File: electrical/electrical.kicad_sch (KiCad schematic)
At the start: 29 parts, among them J1 Raspberry Pi GPIO, J2 Touch screen connector, J3 Load_cell, J4 PIR_sensor, J9 Water_sensor, K1 RAYEX-L90, M1 Milk_powder, M2 Instant_coffee, M3 Sugar, M4 Motor_DC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

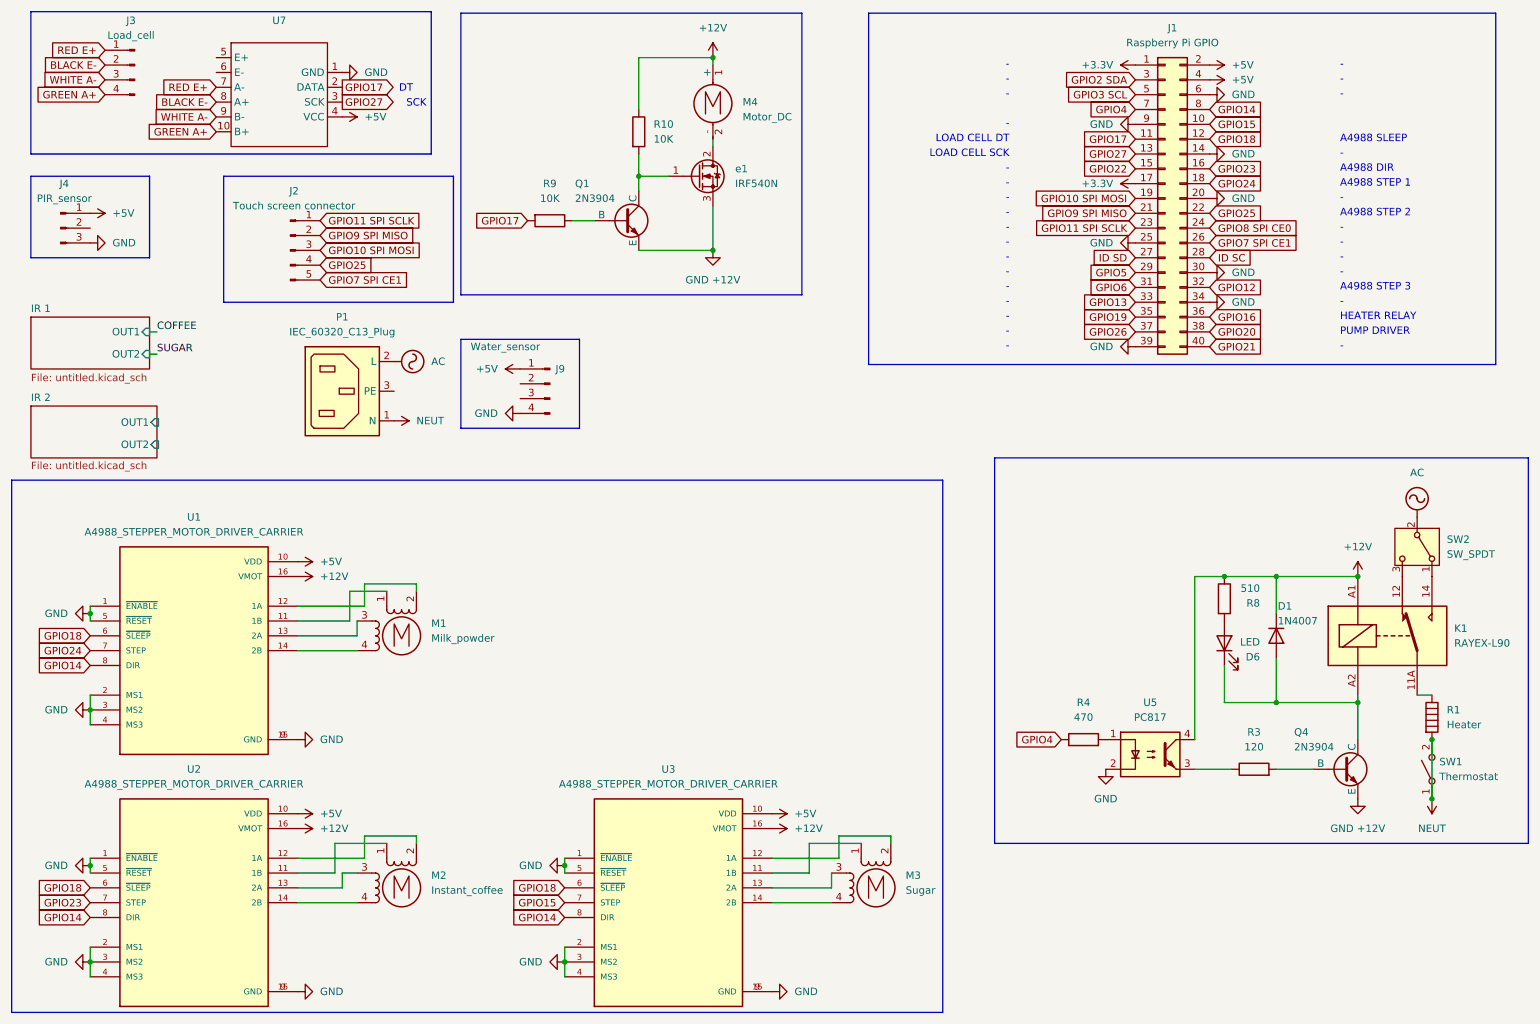
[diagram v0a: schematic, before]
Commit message: added scrolling feature
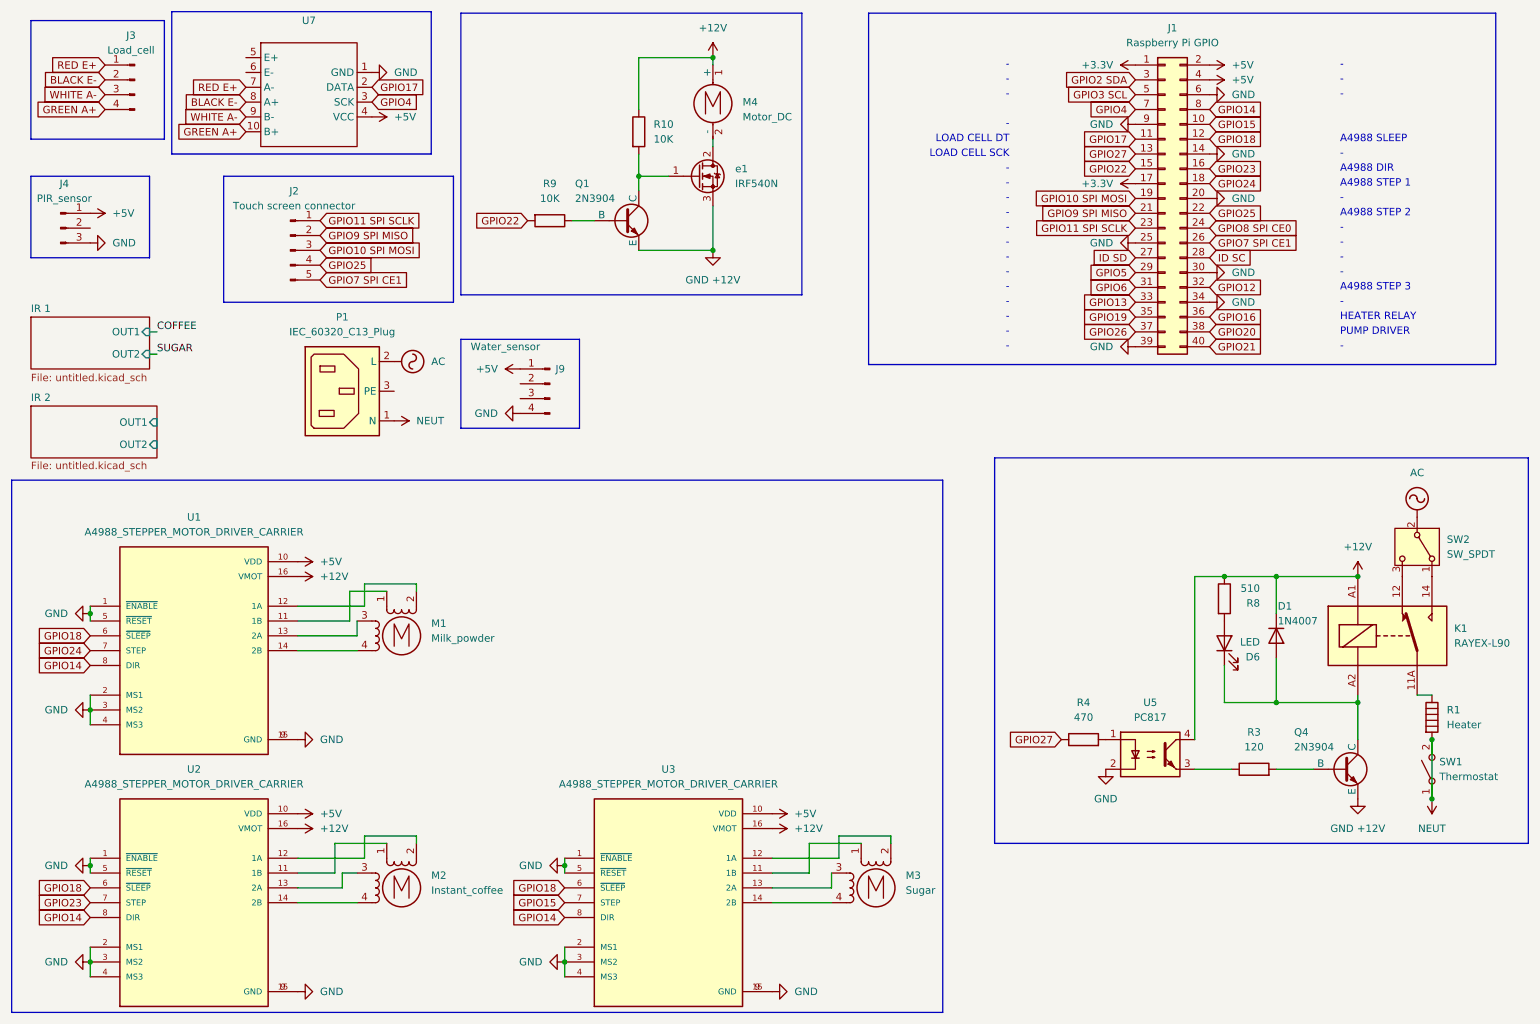
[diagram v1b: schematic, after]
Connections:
- net GPIO17: no longer R9.2
- net GPIO22: now also R9.2
- net GPIO27: now also R4.1; no longer U7.3 (SCK)
- net GPIO4: now also U7.3 (SCK); no longer R4.1
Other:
- note removed: "DT"
- note removed: "SCK"
- moved on the sheet: J3, U7
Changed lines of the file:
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@@
 	)
 	(rectangle
-		(start 19.05 21.336)
+		(start 43.18 21.336)
 		(end 87.63 45.72)
 		(stroke
@@
 	)
 	(rectangle
+		(start 19.05 22.86)
+		(end 41.91 43.18)
+		(stroke
+			(width 0)
+			(type default)
+		)
+		(fill
+			(type none)
+		)
+	)
+	(rectangle
 		(start 15.748 101.6)
 		(end 175.26 192.786)
@@
 		)
 	)
-	(text "DT"
-		(exclude_from_sim no)
-		(at 83.312 34.544 0)
-		(effects
-			(font
-				(size 1.27 1.27)
-			)
-		)
-	)
 	(text "-"
 		(exclude_from_sim no)
@@
 		)
 	)
-	(text "SCK"
-		(exclude_from_sim no)
-		(at 85.09 37.084 0)
-		(effects
-			(font
-				(size 1.27 1.27)
-			)
-		)
-	)
 	(text "-"
 		(exclude_from_sim no)
@@
 	(global_label "GPIO4"
 		(shape input)
-		(at 195.58 146.05 180)
+		(at 77.47 36.83 0)
 		(fields_autoplaced yes)
 		(effects
@@
 				(size 1.27 1.27)
 			)
-			(justify right)
+			(justify left)
 		)
 		(property "Intersheetrefs" "${INTERSHEET_REFS}"
-			(at 186.91 146.05 0)
+			(at 86.14 36.83 0)
 			(effects
 				(font
 					(size 1.27 1.27)
 				)
-				(justify right)
+				(justify left)
 				(hide yes)
 			)
@@
 		)
 	)
-	(global_label "GPIO27"
-		(shape output)
-		(at 72.39 36.83 0)
+	(global_label "GPIO22"
+		(shape input)
+		(at 104.14 57.15 180)
 		(fields_autoplaced yes)
 		(effects
@@
 				(size 1.27 1.27)
 			)
-			(justify left)
+			(justify right)
 		)
 		(property "Intersheetrefs" "${INTERSHEET_REFS}"
-			(at 82.2695 36.83 0)
+			(at 94.2605 57.15 0)
 			(effects
 				(font
 					(size 1.27 1.27)
 				)
-				(justify left)
+				(justify right)
 				(hide yes)
 			)
@@
 	(global_label "BLACK E-"
 		(shape input)
-		(at 31.75 30.48 180)
+		(at 31.75 33.02 180)
 		(fields_autoplaced yes)
 		(effects
@@
 		)
 		(property "Intersheetrefs" "${INTERSHEET_REFS}"
-			(at 19.1491 30.48 0)
+			(at 19.1491 33.02 0)
 			(effects
 				(font
@@
 	(global_label "GREEN A+"
 		(shape input)
-		(at 50.8 41.91 180)
+		(at 55.88 41.91 180)
 		(fields_autoplaced yes)
 		(effects
@@
 		)
 		(property "Intersheetrefs" "${INTERSHEET_REFS}"
-			(at 38.0177 41.91 0)
+			(at 43.0977 41.91 0)
 			(effects
 				(font
@@
 	(global_label "GPIO27"
 		(shape input)
+		(at 195.58 146.05 180)
+		(fields_autoplaced yes)
+		(effects
+			(font
+				(size 1.27 1.27)
+			)
+			(justify right)
+		)
+		(property "Intersheetrefs" "${INTERSHEET_REFS}"
+			(at 185.7005 146.05 0)
+			(effects
+				(font
+					(size 1.27 1.27)
+				)
+				(justify right)
+				(hide yes)
+			)
+		)
+	)
+	(global_label "GPIO27"
+		(shape input)
 		(at 208.28 45.72 180)
 		(fields_autoplaced yes)
@@
 	(global_label "WHITE A-"
 		(shape input)
-		(at 31.75 33.02 180)
+		(at 31.75 35.56 180)
 		(fields_autoplaced yes)
 		(effects
@@
 		)
 		(property "Intersheetrefs" "${INTERSHEET_REFS}"
-			(at 19.6329 33.02 0)
+			(at 19.6329 35.56 0)
 			(effects
 				(font
@@
 	(global_label "GPIO17"
 		(shape input)
-		(at 104.14 57.15 180)
+		(at 77.47 34.29 0)
 		(fields_autoplaced yes)
 		(effects
@@
 				(size 1.27 1.27)
 			)
-			(justify right)
+			(justify left)
 		)
 		(property "Intersheetrefs" "${INTERSHEET_REFS}"
-			(at 94.2605 57.15 0)
+			(at 87.3495 34.29 0)
 			(effects
 				(font
 					(size 1.27 1.27)
 				)
-				(justify right)
+				(justify left)
 				(hide yes)
 			)
@@
 	(global_label "BLACK E-"
 		(shape input)
-		(at 50.8 36.83 180)
+		(at 55.88 36.83 180)
 		(fields_autoplaced yes)
 		(effects
@@
 		)
 		(property "Intersheetrefs" "${INTERSHEET_REFS}"
-			(at 38.1991 36.83 0)
+			(at 43.2791 36.83 0)
 			(effects
 				(font
@@
 	(global_label "RED E+"
 		(shape input)
-		(at 31.75 27.94 180)
+		(at 31.75 30.48 180)
 		(fields_autoplaced yes)
 		(effects
@@
 		)
 		(property "Intersheetrefs" "${INTERSHEET_REFS}"
-			(at 21.3868 27.94 0)
+			(at 21.3868 30.48 0)
 			(effects
 				(font
@@
 	(global_label "WHITE A-"
 		(shape input)
-		(at 50.8 39.37 180)
+		(at 55.88 39.37 180)
 		(fields_autoplaced yes)
 		(effects
@@
 		)
 		(property "Intersheetrefs" "${INTERSHEET_REFS}"
-			(at 38.6829 39.37 0)
+			(at 43.7629 39.37 0)
 			(effects
 				(font
@@
 		)
 	)
-	(global_label "GPIO17"
-		(shape output)
-		(at 72.39 34.29 0)
-		(fields_autoplaced yes)
-		(effects
-			(font
-				(size 1.27 1.27)
-			)
-			(justify left)
-		)
-		(property "Intersheetrefs" "${INTERSHEET_REFS}"
-			(at 82.2695 34.29 0)
-			(effects
-				(font
-					(size 1.27 1.27)
-				)
-				(justify left)
-				(hide yes)
-			)
-		)
-	)
 	(global_label "GPIO10 SPI MOSI"
 		(shape input)
@@
 	(global_label "RED E+"
 		(shape input)
-		(at 50.8 34.29 180)
+		(at 55.88 34.29 180)
 		(fields_autoplaced yes)
 		(effects
@@
 		)
 		(property "Intersheetrefs" "${INTERSHEET_REFS}"
-			(at 40.4368 34.29 0)
+			(at 45.5168 34.29 0)
 			(effects
 				(font
@@
 	(global_label "GREEN A+"
 		(shape input)
-		(at 31.75 35.56 180)
+		(at 31.75 38.1 180)
 		(fields_autoplaced yes)
 		(effects
@@
 		)
 		(property "Intersheetrefs" "${INTERSHEET_REFS}"
-			(at 18.9677 35.56 0)
+			(at 18.9677 38.1 0)
 			(effects
 				(font
@@
 	(symbol
 		(lib_id "power:GND")
-		(at 72.39 31.75 90)
+		(at 77.47 31.75 90)
 		(unit 1)
 		(exclude_from_sim no)
@@
 		(fields_autoplaced yes)
 		(property "Reference" "#PWR017"
-			(at 78.74 31.75 0)
+			(at 83.82 31.75 0)
 			(effects
 				(font
@@
 		)
 		(property "Value" "GND"
-			(at 76.2 31.7499 90)
+			(at 81.28 31.7499 90)
 			(effects
 				(font
@@
 		)
 		(property "Footprint" ""
-			(at 72.39 31.75 0)
+			(at 77.47 31.75 0)
 			(effects
 				(font
@@
 		)
 		(property "Datasheet" ""
-			(at 72.39 31.75 0)
+			(at 77.47 31.75 0)
 			(effects
 				(font
@@
 		)
 		(property "Description" "Power symbol creates a global label with name \"GND\" , ground"
-			(at 72.39 31.75 0)
+			(at 77.47 31.75 0)
 			(effects
 				(font
@@
 	(symbol
 		(lib_id "Connector:Conn_01x04_Pin")
-		(at 36.83 30.48 0)
+		(at 36.83 33.02 0)
 		(mirror y)
 		(unit 1)
@@
 		(dnp no)
 		(property "Reference" "J3"
-			(at 36.195 22.86 0)
+			(at 36.195 25.4 0)
 			(effects
 				(font
@@
 		)
 		(property "Value" "Load_cell"
-			(at 36.195 25.4 0)
+			(at 36.195 27.94 0)
 			(effects
 				(font
@@
 		)
 		(property "Footprint" "Connector_PinHeader_2.54mm:PinHeader_1x04_P2.54mm_Vertical"
-			(at 36.83 30.48 0)
+			(at 36.83 33.02 0)
 			(effects
 				(font
@@
 		)
 		(property "Datasheet" "~"
-			(at 36.83 30.48 0)
+			(at 36.83 33.02 0)
 			(effects
 				(font
@@
 		)
 		(property "Description" "Generic connector, single row, 01x04, script generated"
-			(at 36.83 30.48 0)
+			(at 36.83 33.02 0)
 			(effects
 				(font
@@
 	(symbol
 		(lib_id "hx711:hx711")
-		(at 60.96 35.56 0)
+		(at 66.04 35.56 0)
 		(unit 1)
 		(exclude_from_sim no)
@@
 		(fields_autoplaced yes)
 		(property "Reference" "U7"
-			(at 61.595 22.86 0)
+			(at 66.675 22.86 0)
 			(effects
 				(font
@@
 		)
 		(property "Value" "~"
-			(at 61.595 25.4 0)
+			(at 66.675 25.4 0)
 			(effects
 				(font
@@
 		)
 		(property "Footprint" "Library:HX711"
-			(at 60.96 35.56 0)
+			(at 66.04 35.56 0)
 			(effects
 				(font
@@
 		)
 		(property "Datasheet" ""
-			(at 60.96 35.56 0)
+			(at 66.04 35.56 0)
 			(effects
 				(font
@@
 		)
 		(property "Description" ""
-			(at 60.96 35.56 0)
+			(at 66.04 35.56 0)
 			(effects
 				(font
@@
 	(symbol
 		(lib_id "power:+5V")
-		(at 72.39 39.37 270)
+		(at 77.47 39.37 270)
 		(unit 1)
 		(exclude_from_sim no)
@@
 		(fields_autoplaced yes)
 		(property "Reference" "#PWR018"
-			(at 68.58 39.37 0)
+			(at 73.66 39.37 0)
 			(effects
 				(font
@@
 		)
 		(property "Value" "+5V"
-			(at 76.2 39.3699 90)
+			(at 81.28 39.3699 90)
 			(effects
 				(font
@@
 		)
 		(property "Footprint" ""
-			(at 72.39 39.37 0)
+			(at 77.47 39.37 0)
 			(effects
 				(font
@@
 		)
 		(property "Datasheet" ""
-			(at 72.39 39.37 0)
+			(at 77.47 39.37 0)
 			(effects
 				(font
@@
 		)
 		(property "Description" "Power symbol creates a global label with name \"+5V\""
-			(at 72.39 39.37 0)
+			(at 77.47 39.37 0)
 			(effects
 				(font
@@
 		)
 		(pin "OUT2" input
-			(at 40.894 95.504 0)
+			(at 40.64 95.504 0)
 			(effects
 				(font
@@
 		)
 		(pin "OUT1" input
-			(at 40.894 91.694 0)
+			(at 40.64 91.694 0)
 			(effects
 				(font
